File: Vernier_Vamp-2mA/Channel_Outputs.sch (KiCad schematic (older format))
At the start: 45 parts, among them U12 OPA2277, U13 OPA2277, U14 OPA2277

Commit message: 1.0B fixes for 2mA (schematic)
Added 1.0B fixes to the 2mA version related to schematic cleanup, and addition of hysteresis and alternative way to power nano.
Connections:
- net labels added: +7.5V, -7.5V
- net labels removed: +8V, -8V
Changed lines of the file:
@@
 $Descr A4 11693 8268
 encoding utf-8
-Sheet 5 5
-Title "\"Vernier Vamp\" Coil Driver - 200mA"
-Date "2020-02-04"
-Rev "1.0A"
+Sheet 6 7
+Title "\"Vernier Vamp\" Coil Driver - 2mA"
+Date "2020-05-05"
+Rev "1.0B"
 Comp "Strathclyde University"
 Comment1 "Designed by: Marcin Mrozowski"
@@
 $EndComp
 $Comp
-L power:-8V #PWR?
-U 1 1 61BB20DB
-P 4750 4800
-AR Path="/5E1DD6A9/61BB20DB" Ref="#PWR?"  Part="1"
-AR Path="/5E1E279E/61BB20DB" Ref="#PWR0158"  Part="1"
-F 0 "#PWR0158" H 4750 4900 50  0001 C CNN
-F 1 "-8V" H 4765 4973 50  0000 C CNN
-F 2 "" H 4750 4800 50  0001 C CNN
-F 3 "" H 4750 4800 50  0001 C CNN
-	1    4750 4800
-	-1   0    0    1
-$EndComp
-$Comp
-L power:-8V #PWR?
-U 1 1 61BBF222
-P 4750 2400
-AR Path="/5E1DD6A9/61BBF222" Ref="#PWR?"  Part="1"
-AR Path="/5E1E279E/61BBF222" Ref="#PWR0162"  Part="1"
-F 0 "#PWR0162" H 4750 2500 50  0001 C CNN
-F 1 "-8V" H 4765 2573 50  0000 C CNN
-F 2 "" H 4750 2400 50  0001 C CNN
-F 3 "" H 4750 2400 50  0001 C CNN
-	1    4750 2400
-	-1   0    0    1
-$EndComp
-$Comp
-L power:-8V #PWR?
-U 1 1 61BE659B
-P 4750 7200
-AR Path="/5E1DD6A9/61BE659B" Ref="#PWR?"  Part="1"
-AR Path="/5E1E279E/61BE659B" Ref="#PWR0171"  Part="1"
-F 0 "#PWR0171" H 4750 7300 50  0001 C CNN
-F 1 "-8V" H 4765 7373 50  0000 C CNN
-F 2 "" H 4750 7200 50  0001 C CNN
-F 3 "" H 4750 7200 50  0001 C CNN
-	1    4750 7200
-	-1   0    0    1
-$EndComp
-$Comp
-L power:-8V #PWR?
-U 1 1 61C00694
-P 1000 7550
-AR Path="/5E1DD6A9/61C00694" Ref="#PWR?"  Part="1"
-AR Path="/5E1E279E/61C00694" Ref="#PWR0173"  Part="1"
-F 0 "#PWR0173" H 1000 7650 50  0001 C CNN
-F 1 "-8V" H 1015 7723 50  0000 C CNN
-F 2 "" H 1000 7550 50  0001 C CNN
-F 3 "" H 1000 7550 50  0001 C CNN
-	1    1000 7550
-	-1   0    0    1
-$EndComp
-$Comp
-L power:+8V #PWR?
-U 1 1 61CC3835
-P 4750 1800
-AR Path="/5E1DD6A9/61CC3835" Ref="#PWR?"  Part="1"
-AR Path="/5E1E279E/61CC3835" Ref="#PWR0177"  Part="1"
-F 0 "#PWR0177" H 4750 1650 50  0001 C CNN
-F 1 "+8V" H 4765 1973 50  0000 C CNN
-F 2 "" H 4750 1800 50  0001 C CNN
-F 3 "" H 4750 1800 50  0001 C CNN
-	1    4750 1800
-	1    0    0    -1
-$EndComp
-$Comp
-L power:+8V #PWR?
-U 1 1 61D1FDE2
-P 4750 4200
-AR Path="/5E1DD6A9/61D1FDE2" Ref="#PWR?"  Part="1"
-AR Path="/5E1E279E/61D1FDE2" Ref="#PWR0182"  Part="1"
-F 0 "#PWR0182" H 4750 4050 50  0001 C CNN
-F 1 "+8V" H 4765 4373 50  0000 C CNN
-F 2 "" H 4750 4200 50  0001 C CNN
-F 3 "" H 4750 4200 50  0001 C CNN
-	1    4750 4200
-	1    0    0    -1
-$EndComp
-$Comp
-L power:+8V #PWR?
-U 1 1 61D53ED0
-P 1050 6250
-AR Path="/5E1DD6A9/61D53ED0" Ref="#PWR?"  Part="1"
-AR Path="/5E1E279E/61D53ED0" Ref="#PWR0184"  Part="1"
-F 0 "#PWR0184" H 1050 6100 50  0001 C CNN
-F 1 "+8V" H 1065 6423 50  0000 C CNN
-F 2 "" H 1050 6250 50  0001 C CNN
-F 3 "" H 1050 6250 50  0001 C CNN
-	1    1050 6250
-	1    0    0    -1
-$EndComp
-$Comp
-L power:+8V #PWR?
-U 1 1 61D8B028
-P 4750 6600
-AR Path="/5E1DD6A9/61D8B028" Ref="#PWR?"  Part="1"
-AR Path="/5E1E279E/61D8B028" Ref="#PWR0185"  Part="1"
-F 0 "#PWR0185" H 4750 6450 50  0001 C CNN
-F 1 "+8V" H 4765 6773 50  0000 C CNN
-F 2 "" H 4750 6600 50  0001 C CNN
-F 3 "" H 4750 6600 50  0001 C CNN
-	1    4750 6600
-	1    0    0    -1
-$EndComp
-$Comp
 L Connector:TestPoint_Probe TP?
 U 1 1 627595FD
@@
 	6750 750  6750 1050
 Connection ~ 6750 1050
+$Comp
+L custom_power_rails:+7.5V #PWR?
+U 1 1 5EFDFA63
+P 1050 6250
+AR Path="/5E1DD6A9/5EC279B2/5EFDFA63" Ref="#PWR?"  Part="1"
+AR Path="/5E1E279E/5EFDFA63" Ref="#PWR0184"  Part="1"
+F 0 "#PWR0184" H 1050 6200 50  0001 C CNN
+F 1 "+7.5V" H 1035 6423 50  0000 C CNN
+F 2 "" H 1050 6250 50  0001 C CNN
+F 3 "" H 1050 6250 50  0001 C CNN
+	1    1050 6250
+	1    0    0    -1
+$EndComp
+$Comp
+L custom_power_rails:+7.5V #PWR?
+U 1 1 5EFE4517
+P 4750 6600
+AR Path="/5E1DD6A9/5EC279B2/5EFE4517" Ref="#PWR?"  Part="1"
+AR Path="/5E1E279E/5EFE4517" Ref="#PWR0185"  Part="1"
+F 0 "#PWR0185" H 4750 6550 50  0001 C CNN
+F 1 "+7.5V" H 4735 6773 50  0000 C CNN
+F 2 "" H 4750 6600 50  0001 C CNN
+F 3 "" H 4750 6600 50  0001 C CNN
+	1    4750 6600
+	1    0    0    -1
+$EndComp
+$Comp
+L custom_power_rails:+7.5V #PWR?
+U 1 1 5EFE9018
+P 4750 4200
+AR Path="/5E1DD6A9/5EC279B2/5EFE9018" Ref="#PWR?"  Part="1"
+AR Path="/5E1E279E/5EFE9018" Ref="#PWR0197"  Part="1"
+F 0 "#PWR0197" H 4750 4150 50  0001 C CNN
+F 1 "+7.5V" H 4735 4373 50  0000 C CNN
+F 2 "" H 4750 4200 50  0001 C CNN
+F 3 "" H 4750 4200 50  0001 C CNN
+	1    4750 4200
+	1    0    0    -1
+$EndComp
+$Comp
+L custom_power_rails:+7.5V #PWR?
+U 1 1 5EFEDB22
+P 4750 1800
+AR Path="/5E1DD6A9/5EC279B2/5EFEDB22" Ref="#PWR?"  Part="1"
+AR Path="/5E1E279E/5EFEDB22" Ref="#PWR0198"  Part="1"
+F 0 "#PWR0198" H 4750 1750 50  0001 C CNN
+F 1 "+7.5V" H 4735 1973 50  0000 C CNN
+F 2 "" H 4750 1800 50  0001 C CNN
+F 3 "" H 4750 1800 50  0001 C CNN
+	1    4750 1800
+	1    0    0    -1
+$EndComp
+$Comp
+L custom_power_rails:-7.5V #PWR?
+U 1 1 5F0497FE
+P 1000 7550
+AR Path="/5E1DD6A9/5EC279B2/5F0497FE" Ref="#PWR?"  Part="1"
+AR Path="/5E1DD6A9/5F0497FE" Ref="#PWR?"  Part="1"
+AR Path="/5E1E279E/5F0497FE" Ref="#PWR0199"  Part="1"
+F 0 "#PWR0199" H 1000 7500 50  0001 C CNN
+F 1 "-7.5V" H 985 7723 50  0000 C CNN
+F 2 "" H 1000 7550 50  0001 C CNN
+F 3 "" H 1000 7550 50  0001 C CNN
+	1    1000 7550
+	-1   0    0    1
+$EndComp
+$Comp
+L custom_power_rails:-7.5V #PWR?
+U 1 1 5F0528F2
+P 4750 2400
+AR Path="/5E1DD6A9/5EC279B2/5F0528F2" Ref="#PWR?"  Part="1"
+AR Path="/5E1DD6A9/5F0528F2" Ref="#PWR?"  Part="1"
+AR Path="/5E1E279E/5F0528F2" Ref="#PWR0200"  Part="1"
+F 0 "#PWR0200" H 4750 2350 50  0001 C CNN
+F 1 "-7.5V" H 4735 2573 50  0000 C CNN
+F 2 "" H 4750 2400 50  0001 C CNN
+F 3 "" H 4750 2400 50  0001 C CNN
+	1    4750 2400
+	-1   0    0    1
+$EndComp
+$Comp
+L custom_power_rails:-7.5V #PWR?
+U 1 1 5F0571F5
+P 4750 4800
+AR Path="/5E1DD6A9/5EC279B2/5F0571F5" Ref="#PWR?"  Part="1"
+AR Path="/5E1DD6A9/5F0571F5" Ref="#PWR?"  Part="1"
+AR Path="/5E1E279E/5F0571F5" Ref="#PWR0203"  Part="1"
+F 0 "#PWR0203" H 4750 4750 50  0001 C CNN
+F 1 "-7.5V" H 4735 4973 50  0000 C CNN
+F 2 "" H 4750 4800 50  0001 C CNN
+F 3 "" H 4750 4800 50  0001 C CNN
+	1    4750 4800
+	-1   0    0    1
+$EndComp
+$Comp
+L custom_power_rails:-7.5V #PWR?
+U 1 1 5F060C92
+P 4750 7200
+AR Path="/5E1DD6A9/5EC279B2/5F060C92" Ref="#PWR?"  Part="1"
+AR Path="/5E1DD6A9/5F060C92" Ref="#PWR?"  Part="1"
+AR Path="/5E1E279E/5F060C92" Ref="#PWR0204"  Part="1"
+F 0 "#PWR0204" H 4750 7150 50  0001 C CNN
+F 1 "-7.5V" H 4735 7373 50  0000 C CNN
+F 2 "" H 4750 7200 50  0001 C CNN
+F 3 "" H 4750 7200 50  0001 C CNN
+	1    4750 7200
+	-1   0    0    1
+$EndComp
 $EndSCHEMATC

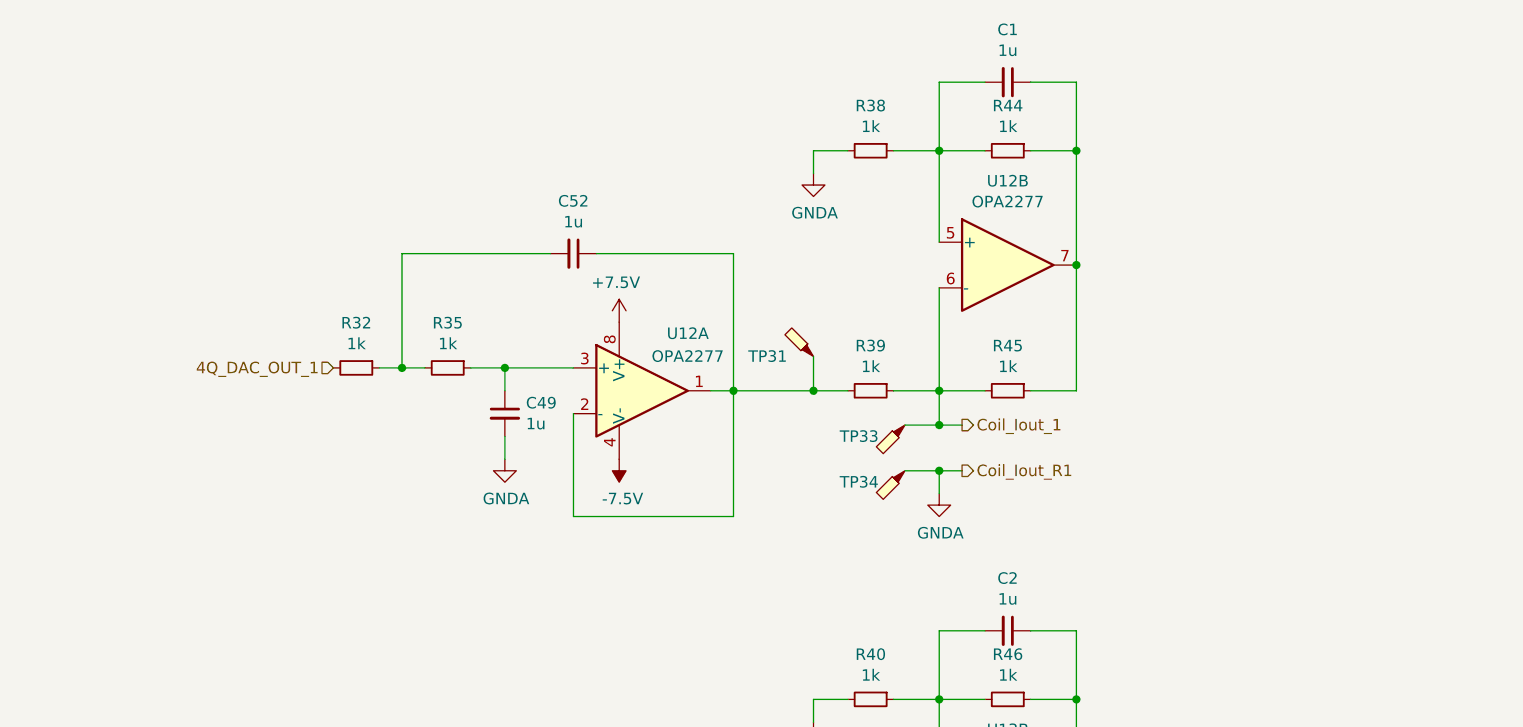
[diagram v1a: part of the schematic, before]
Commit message: Applied 1.0B changes to 2mA version
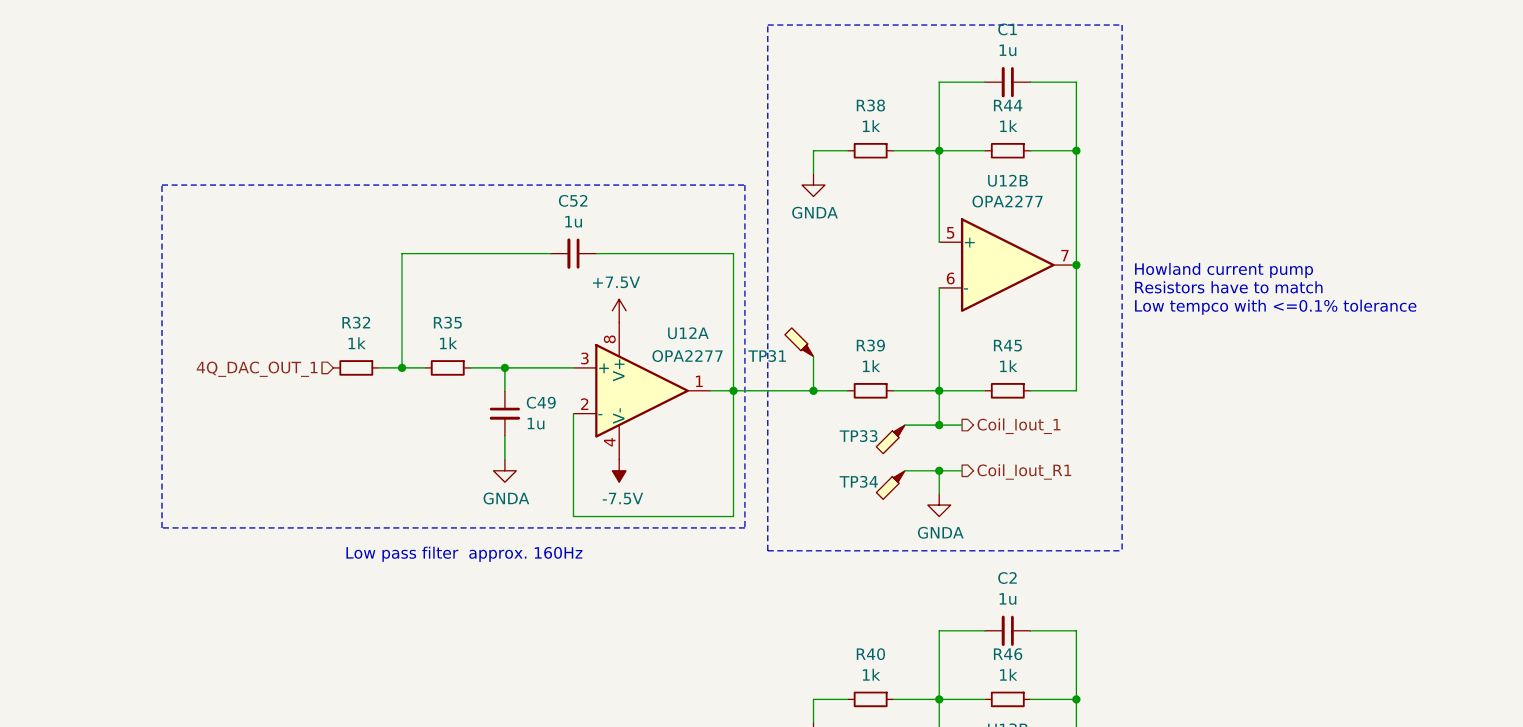
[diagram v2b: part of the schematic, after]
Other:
- note added: "Howland current pump\nResistors have to match\nLow tempco with <=0.1% tolerance\n\n"
- note added: "Low pass filter approx. 160Hz"
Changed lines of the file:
@@
 	-1   0    0    1
 $EndComp
+Wire Notes Line
+	2750 1200 5300 1200
+Wire Notes Line
+	5300 1200 5300 2700
+Wire Notes Line
+	5300 2700 2750 2700
+Wire Notes Line
+	2750 2700 2750 1200
+Wire Notes Line
+	5400 2800 5400 500
+Wire Notes Line
+	5400 500  6950 500
+Wire Notes Line
+	6950 500  6950 2800
+Wire Notes Line
+	5400 2800 6950 2800
+Text Notes 3550 2850 0    50   ~ 0
+Low pass filter  approx. 160Hz
+Text Notes 7000 1850 0    50   ~ 0
+Howland current pump\nResistors have to match\nLow tempco with <=0.1% tolerance\n\n
 $EndSCHEMATC
